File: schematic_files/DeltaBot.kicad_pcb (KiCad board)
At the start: 2 copper layers, 241.5 x 110.5 mm, 30 parts, among them J1 USB C PD Modulle, J2 LIDAR, J3 MOTOR_L, J4 MOTOR_R, SW1 SW_SPDT, U1 Radxa_ROCK5B, U2 Buck Converter

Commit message: pcb 1st iteration
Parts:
- removed D1, D2: D, deltabot:D_DO-41_SOD81_P10.16mm_Horizontal
- removed J2: LIDAR, deltabot:PinHeader_1x07_P2.54mm_Vertical
- removed REF** (x13), REF\: MountingHole_3.5mm, MountingHole:MountingHole_3.5mm
- added C7: 5uF, Capacitor_SMD:C_0805_2012Metric, F.Cu at (152.3, 93.7)
- added J5: C1_LIDAR, deltabot:C1 LiDAR, F.Cu at (177.7, 105.6)
- C1: footprint deltabot:CP_Radial_D12.5mm_P5.00mm -> Capacitor_THT:CP_Radial_D12.5mm_P5.00mm
- C2, C4, C5, C6: footprint deltabot:C_Disc_D3.0mm_W2.0mm_P2.50mm -> Capacitor_SMD:C_0603_1608Metric
- C3: value 1uF -> 0.1uF; footprint deltabot:C_Disc_D3.0mm_W2.0mm_P2.50mm -> Capacitor_SMD:C_0603_1608Metric
- J1: footprint deltabot:USB_C -> deltabot:USB_PD
- moved J4 91.8 mm to (152.5, 144.1), turned to 90 degrees
- moved C4 83.9 mm to (154.3, 140.3)
- moved C2 81.3 mm to (152.5, 101.6), turned to 180 degrees
- moved C1 73.8 mm to (161.9, 89.4), turned to -90 degrees
- moved C5 68.0 mm to (157.3, 74.0), turned to 180 degrees
- moved J3 64.3 mm to (155.5, 70.1), turned to 90 degrees
- moved C3 47.3 mm to (152.4, 97.6), turned to 180 degrees
- moved U2 33.2 mm to (196.1, 86.7), turned to 180 degrees
- moved F1 28.4 mm to (193.9, 93.4), turned to 180 degrees
- moved SW1 18.2 mm to (190.0, 120.4), turned to -90 degrees
- moved J1 12.7 mm to (157.0, 135.9), turned to 90 degrees
- moved U1 10.6 mm to (90.5, 107.5)
- moved C6 9.19 mm to (52.1, 66.6), turned to 0 degrees
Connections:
- U1 pad 10: LIDAR_RX -> LIDAR_TX
- U1 pad 18: MOTO_CTRL -> unconnected-(U1-GPIO4_D4-Pad18)
- U1 pad 8: LIDAR_TX -> LIDAR_RX
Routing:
- net MOTO_CTRL: track 99.9 -> 0.00 mm, vias 1 -> 0
- net +5V: track 329.1 -> 237.2 mm, vias 1 -> 0
- net PWM_L: track 124.7 -> 170.5 mm, vias 1 -> 0
- net Net-(D2-K): track 35.8 -> 0.00 mm
- net Net-(SW1-B): track 72.0 -> 38.7 mm
- net +9V: track 65.3 -> 33.9 mm
- net LIDAR_TX: track 128.5 -> 105.6 mm, vias 1 -> 0
- net GND: track 11.4 -> 0.00 mm, vias 16 -> 3
- net Net-(J1-VCC): track 20.0 -> 9.92 mm
- net Net-(D1-K): track 5.92 -> 0.00 mm
- net LIDAR_RX: track 112.6 -> 108.3 mm, vias 1 -> 0
- net PWM_R: track 110.4 -> 108.7 mm, vias 1 -> 0
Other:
- board size 241.5 x 110.5 mm -> 175 x 98 mm
- board text removed: "+5V"
- board text removed: "+8.34V"
- board text removed: "+9V"
- board text removed: "Delta-Bot"
- board text removed: "LIDAR_RX"
- board text removed: "LIDAR_TX"
- board text removed: "MOTOR_CTRL"
- board text removed: "OFF"
- board text removed: "ON"
- board text removed: "PWM_L"
- board text removed: "PWM_R"
- board text removed: "SA"
- board text removed: "SERVO_L"
- board text removed: "SERVO_R"
- board text removed: "Δ"

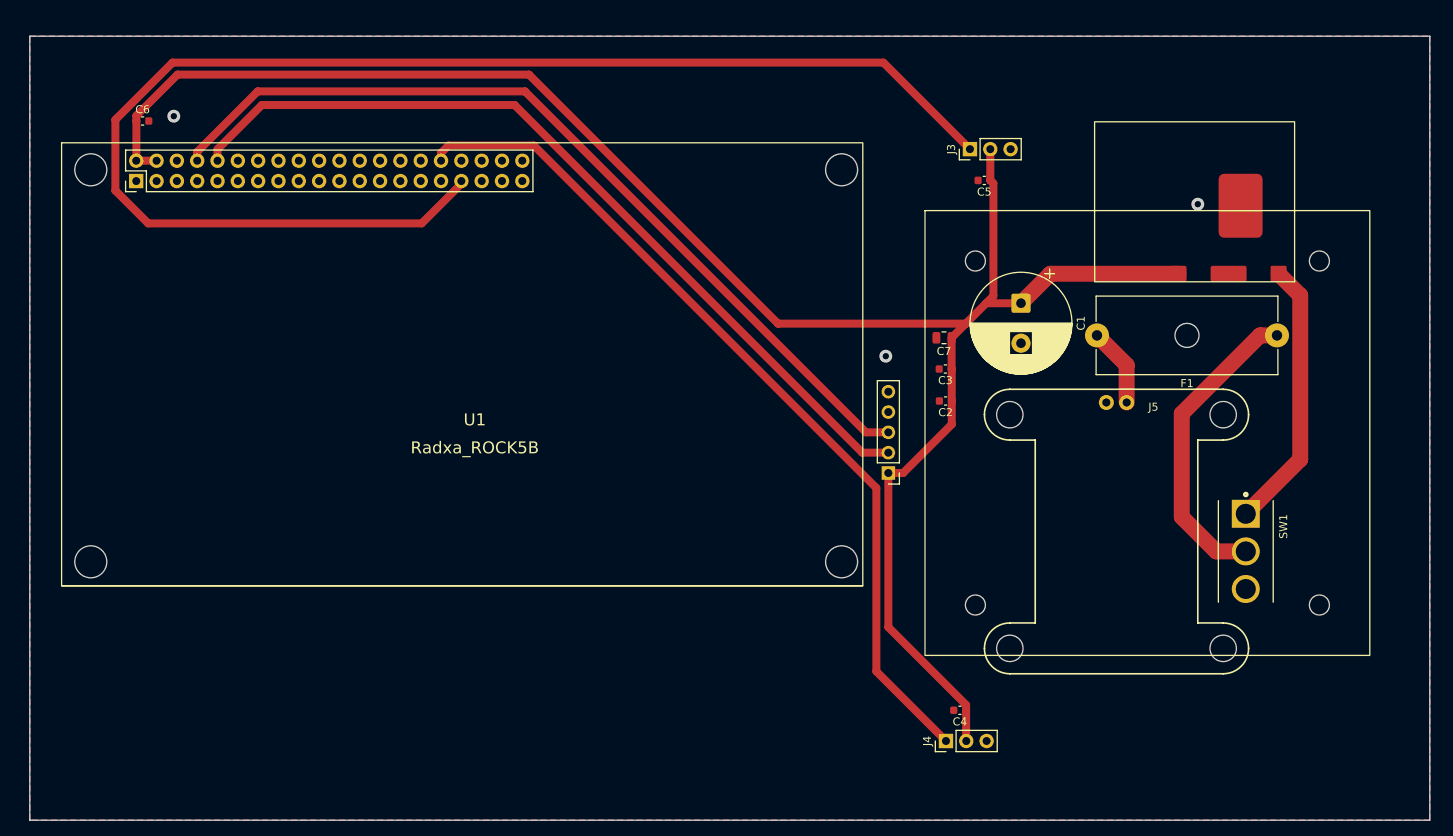
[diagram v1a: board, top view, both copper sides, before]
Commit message: drill holes added for battery pack platform and edgecuts for ports
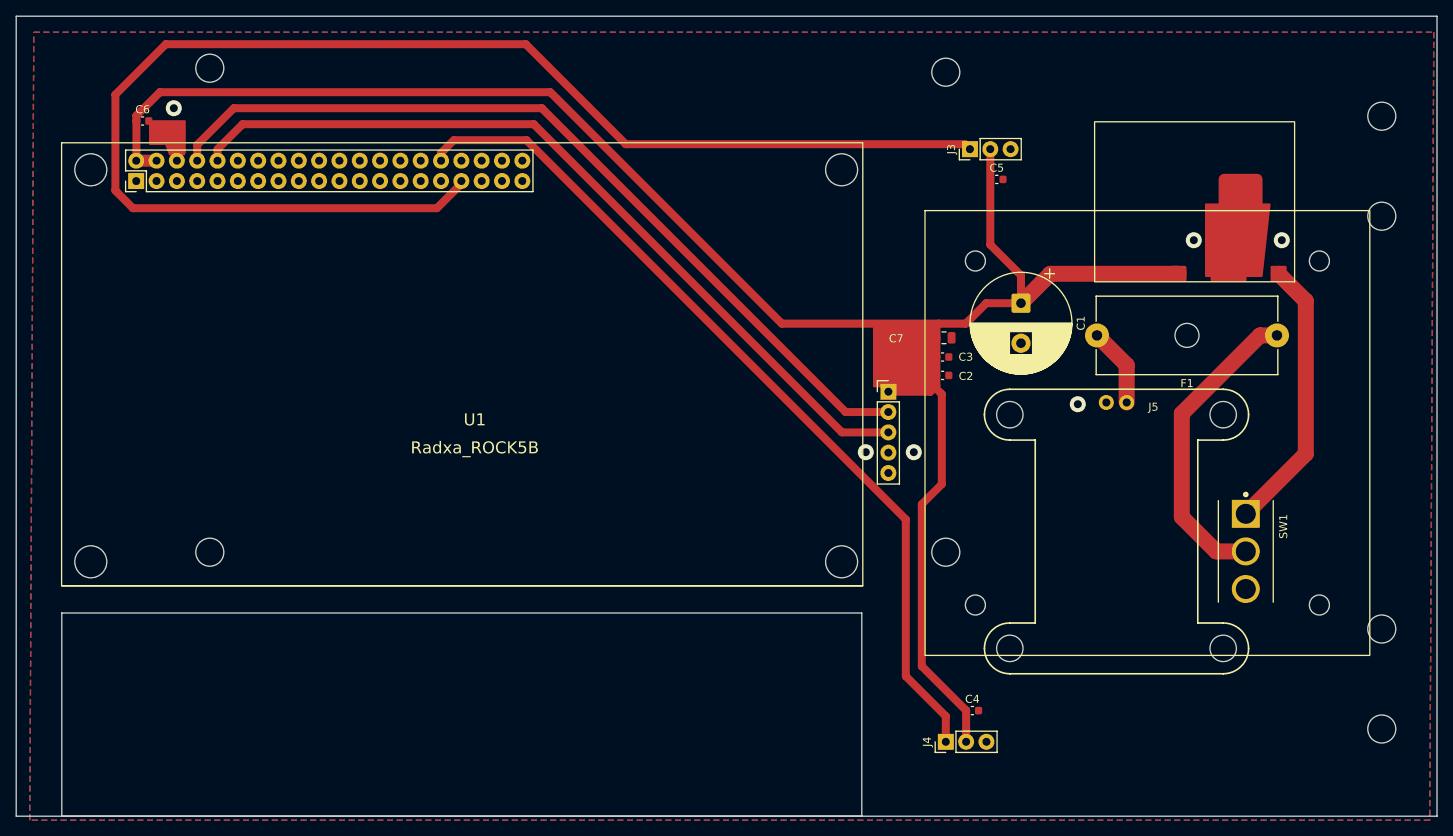
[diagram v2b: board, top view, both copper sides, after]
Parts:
- added REF**: MountingHole_3.5mm, MountingHole:MountingHole_3.5mm, F.Cu at (152.5, 120.5)
- added REF**: MountingHole_3.5mm, MountingHole:MountingHole_3.5mm, F.Cu at (207.0, 78.5)
- added REF**: MountingHole_3.5mm, MountingHole:MountingHole_3.5mm, F.Cu at (152.5, 60.5)
- added REF**: MountingHole_3.5mm, MountingHole:MountingHole_3.5mm, F.Cu at (60.5, 120.5)
- added REF**: MountingHole_3.5mm, MountingHole:MountingHole_3.5mm, F.Cu at (207.0, 142.6)
- added REF**: MountingHole_3.5mm, MountingHole:MountingHole_3.5mm, F.Cu at (207.0, 66.0)
- added REF**: MountingHole_3.5mm, MountingHole:MountingHole_3.5mm, F.Cu at (207.0, 130.1)
- added REF**: MountingHole_3.5mm, MountingHole:MountingHole_3.5mm, F.Cu at (60.5, 60.0)
- moved C2 3.22 mm to (152.1, 98.4), turned to 0 degrees
- moved C5 1.57 mm to (158.9, 73.9), turned to 0 degrees
- moved C4 1.56 mm to (155.8, 140.3), turned to 0 degrees
- moved C3 1.54 mm to (152.1, 96.1), turned to 0 degrees
- moved J4 0.10 mm to (152.5, 144.2)
- turned C7 to 0 degrees
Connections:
- U1 pad 10: LIDAR_TX -> LIDAR_RX
- U1 pad 8: LIDAR_RX -> LIDAR_TX
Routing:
- net LIDAR_RX: track 108.3 -> 102.5 mm
- net +5V: track 237.2 -> 242.2 mm
- net PWM_L: track 170.5 -> 172.6 mm
- net +9V: track 33.9 -> 34.5 mm
- net GND: vias 3 -> 6
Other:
- board size 175 x 98 mm -> 177.6 x 100 mm
